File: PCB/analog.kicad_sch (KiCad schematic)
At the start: 18 parts, among them J1 BNC, J2 BNC, U1 MCP6002-xMC, U2 MCP6002-xMC

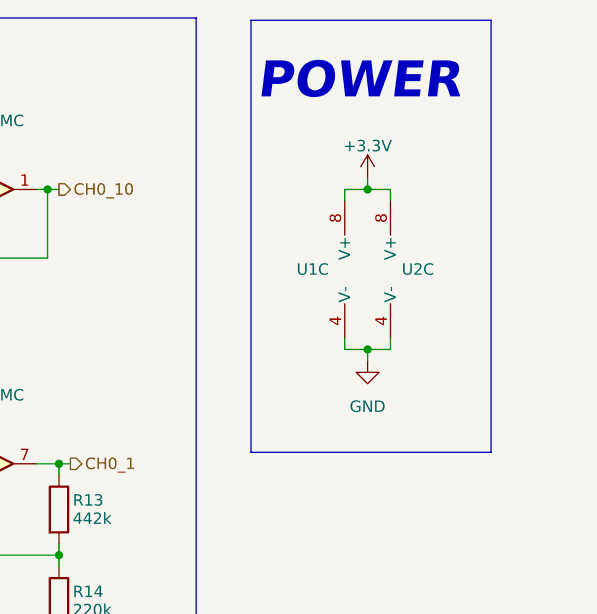
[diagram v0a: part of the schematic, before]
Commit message: add better ground vias; rename footprints and 3d-models
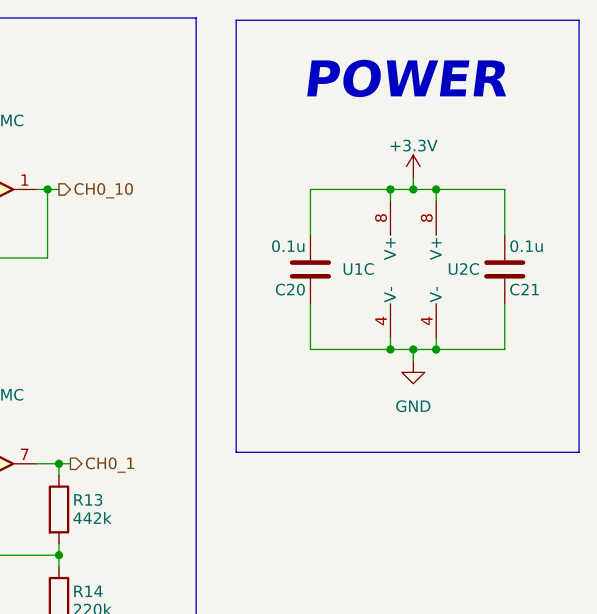
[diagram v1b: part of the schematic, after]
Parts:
- added C20, C21: 0.1u, Capacitor_SMD:C_0603_1608Metric, symbol Device:C
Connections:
- net +3.3V: now also C20.2, C21.2
- net GND: now also C20.1, C21.1
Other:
- moved on the sheet: U1C, U2C

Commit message: remove unneeded pin; update invalid footprint
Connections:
- net GND: no longer U1.9 (V-), U2.9 (V-)
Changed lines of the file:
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@@
 	)
 	(symbol
+		(lib_name "MCP6002-xMC_1")
 		(lib_id "Amplifier_Operational:MCP6002-xMC")
 		(at 175.26 52.07 0)
@@
 		(pin "4"
 		)
-		(pin "9"
-		)
 		(instances
 			(project "oscilloscope"
@@
 	)
 	(symbol
+		(lib_name "MCP6002-xMC_5")
 		(lib_id "Amplifier_Operational:MCP6002-xMC")
 		(at 130.81 124.46 0)
@@
 		(fields_autoplaced yes)
 		(property "Reference" "U2"
-			(at 130.81 114.3 0)
+			(at 131.318 124.46 0)
 			(effects
 				(font
@@
 		)
 		(property "Value" "MCP6002-xMC"
-			(at 130.81 116.84 0)
-			(effects
-				(font
-					(size 1.27 1.27)
-				)
+			(at 130.302 124.46 90)
+			(effects
+				(font
+					(size 1.27 1.27)
+				)
+				(hide yes)
 			)
 		)
@@
 		)
 		(pin "2"
-		)
-		(pin "9"
 		)
 		(instances
@@
 		(fields_autoplaced yes)
 		(property "Reference" "U2"
-			(at 130.81 144.78 0)
+			(at 131.318 154.94 0)
 			(effects
 				(font
@@
 		)
 		(property "Value" "MCP6002-xMC"
-			(at 130.81 147.32 0)
-			(effects
-				(font
-					(size 1.27 1.27)
-				)
+			(at 130.302 154.94 90)
+			(effects
+				(font
+					(size 1.27 1.27)
+				)
+				(hide yes)
 			)
 		)
@@
 		)
 		(pin "2"
-		)
-		(pin "9"
 		)
 		(instances
@@
 	)
 	(symbol
+		(lib_name "MCP6002-xMC_4")
 		(lib_id "Amplifier_Operational:MCP6002-xMC")
 		(at 185.42 52.07 0)
@@
 		(pin "4"
 		)
-		(pin "9"
-		)
 		(instances
 			(project "oscilloscope"
@@
 	)
 	(symbol
+		(lib_name "MCP6002-xMC_3")
 		(lib_id "Amplifier_Operational:MCP6002-xMC")
 		(at 130.81 43.18 0)
@@
 		(fields_autoplaced yes)
 		(property "Reference" "U1"
-			(at 130.81 33.02 0)
+			(at 131.826 43.18 0)
 			(effects
 				(font
@@
 		)
 		(property "Value" "MCP6002-xMC"
-			(at 130.81 35.56 0)
-			(effects
-				(font
-					(size 1.27 1.27)
-				)
+			(at 131.318 43.18 90)
+			(effects
+				(font
+					(size 1.27 1.27)
+				)
+				(hide yes)
 			)
 		)
@@
 		(pin "2"
 		)
-		(pin "9"
-		)
 		(instances
 			(project "oscilloscope"
@@
 	)
 	(symbol
+		(lib_name "MCP6002-xMC_2")
 		(lib_id "Amplifier_Operational:MCP6002-xMC")
 		(at 130.81 73.66 0)
@@
 		(fields_autoplaced yes)
 		(property "Reference" "U1"
-			(at 130.81 63.5 0)
+			(at 131.826 73.66 0)
 			(effects
 				(font
@@
 		)
 		(property "Value" "MCP6002-xMC"
-			(at 130.81 66.04 0)
-			(effects
-				(font
-					(size 1.27 1.27)
-				)
+			(at 131.318 73.66 90)
+			(effects
+				(font
+					(size 1.27 1.27)
+				)
+				(hide yes)
 			)
 		)
@@
 		(pin "2"
 		)
-		(pin "9"
-		)
-		(instances
+		(instances

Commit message: resolve symbol, footprint issues
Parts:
- U1, U2: symbol Amplifier_Operational:MCP6002-xMC -> customLib:MCP6002-xMC
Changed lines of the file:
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@@
 	)
 	(symbol
-		(lib_name "MCP6002-xMC_1")
-		(lib_id "Amplifier_Operational:MCP6002-xMC")
+		(lib_id "customLib:MCP6002-xMC")
 		(at 175.26 52.07 0)
 		(mirror y)
@@
 	)
 	(symbol
-		(lib_name "MCP6002-xMC_5")
-		(lib_id "Amplifier_Operational:MCP6002-xMC")
+		(lib_name "MCP6002-xMC_1")
+		(lib_id "customLib:MCP6002-xMC")
 		(at 130.81 124.46 0)
 		(unit 1)
@@
 		(fields_autoplaced yes)
 		(property "Reference" "U2"
-			(at 131.318 124.46 0)
+			(at 130.81 116.84 0)
 			(effects
 				(font
@@
 	)
 	(symbol
-		(lib_id "Amplifier_Operational:MCP6002-xMC")
+		(lib_name "MCP6002-xMC_3")
+		(lib_id "customLib:MCP6002-xMC")
 		(at 130.81 154.94 0)
 		(unit 2)
@@
 		(fields_autoplaced yes)
 		(property "Reference" "U2"
-			(at 131.318 154.94 0)
+			(at 130.81 147.32 0)
 			(effects
 				(font
@@
 	(symbol
 		(lib_name "MCP6002-xMC_4")
-		(lib_id "Amplifier_Operational:MCP6002-xMC")
+		(lib_id "customLib:MCP6002-xMC")
 		(at 185.42 52.07 0)
 		(unit 3)
@@
 	)
 	(symbol
-		(lib_name "MCP6002-xMC_3")
-		(lib_id "Amplifier_Operational:MCP6002-xMC")
+		(lib_id "customLib:MCP6002-xMC")
 		(at 130.81 43.18 0)
 		(unit 1)
@@
 		(fields_autoplaced yes)
 		(property "Reference" "U1"
-			(at 131.826 43.18 0)
+			(at 130.81 35.56 0)
 			(effects
 				(font
@@
 	)
 	(symbol
-		(lib_name "MCP6002-xMC_2")
-		(lib_id "Amplifier_Operational:MCP6002-xMC")
+		(lib_id "customLib:MCP6002-xMC")
 		(at 130.81 73.66 0)
 		(unit 2)
@@
 		(fields_autoplaced yes)
 		(property "Reference" "U1"
-			(at 131.826 73.66 0)
-			(effects
-				(font
+			(at 130.81 66.04 0)
+			(effects
+				(font

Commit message: resolve footprint issues
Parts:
- R10, R6: LCSC C100970 -> C23137
- R11: LCSC C103831 -> C23254
- R14, R5, R9: LCSC C123420 -> C22961
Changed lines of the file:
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@@
 			)
 		)
-		(property "LCSC" "C123420"
+		(property "LCSC" " C22961"
 			(at 110.49 116.84 0)
 			(effects
@@
 			)
 		)
-		(property "LCSC" "C103831"
+		(property "LCSC" " C23254"
 			(at 110.49 147.32 0)
 			(effects
@@
 			)
 		)
-		(property "LCSC" "C123420"
+		(property "LCSC" " C22961"
 			(at 140.97 88.9 0)
 			(effects
@@
 			)
 		)
-		(property "LCSC" "C100970"
+		(property "LCSC" "C23137"
 			(at 110.49 45.72 0)
 			(effects
@@
 			)
 		)
-		(property "LCSC" "C100970"
+		(property "LCSC" "C23137"
 			(at 110.49 127 0)
 			(effects
@@
 			)
 		)
-		(property "LCSC" "C123420"
+		(property "LCSC" " C22961"
 			(at 110.49 35.56 0)
 			(effects
